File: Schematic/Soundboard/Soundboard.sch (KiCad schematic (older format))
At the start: 0 parts

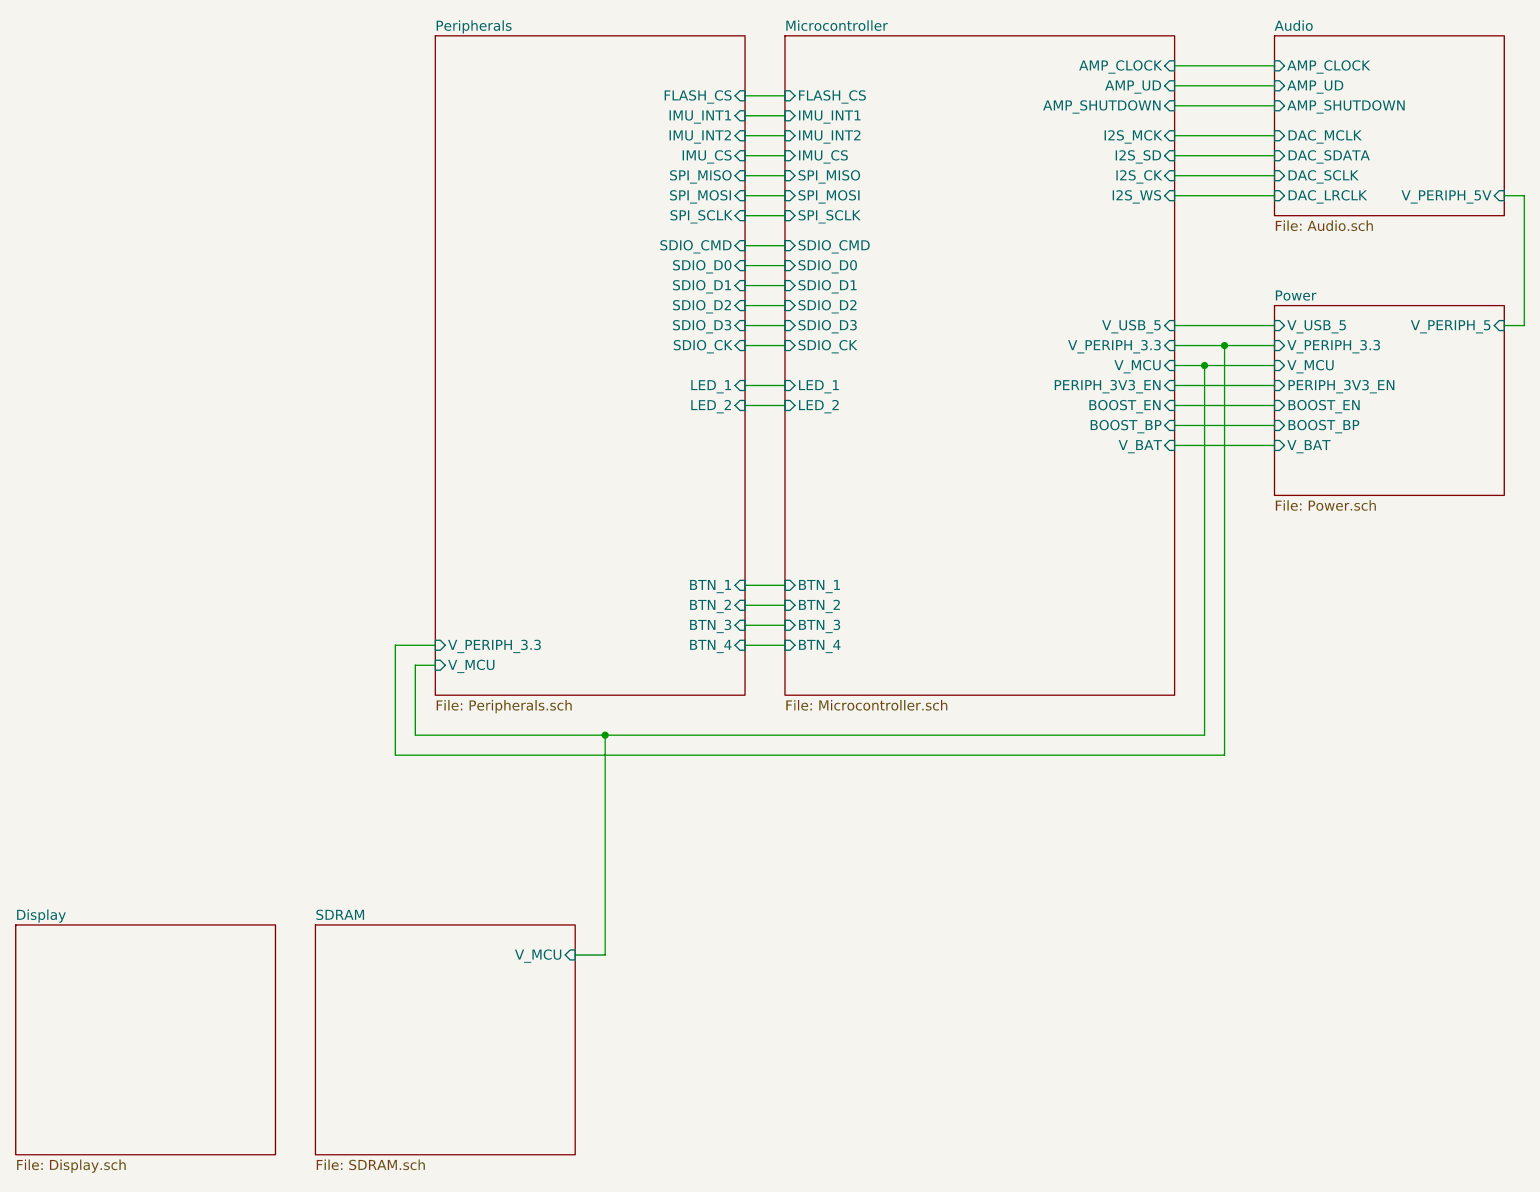
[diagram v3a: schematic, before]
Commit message: Choose display. Complete schematic
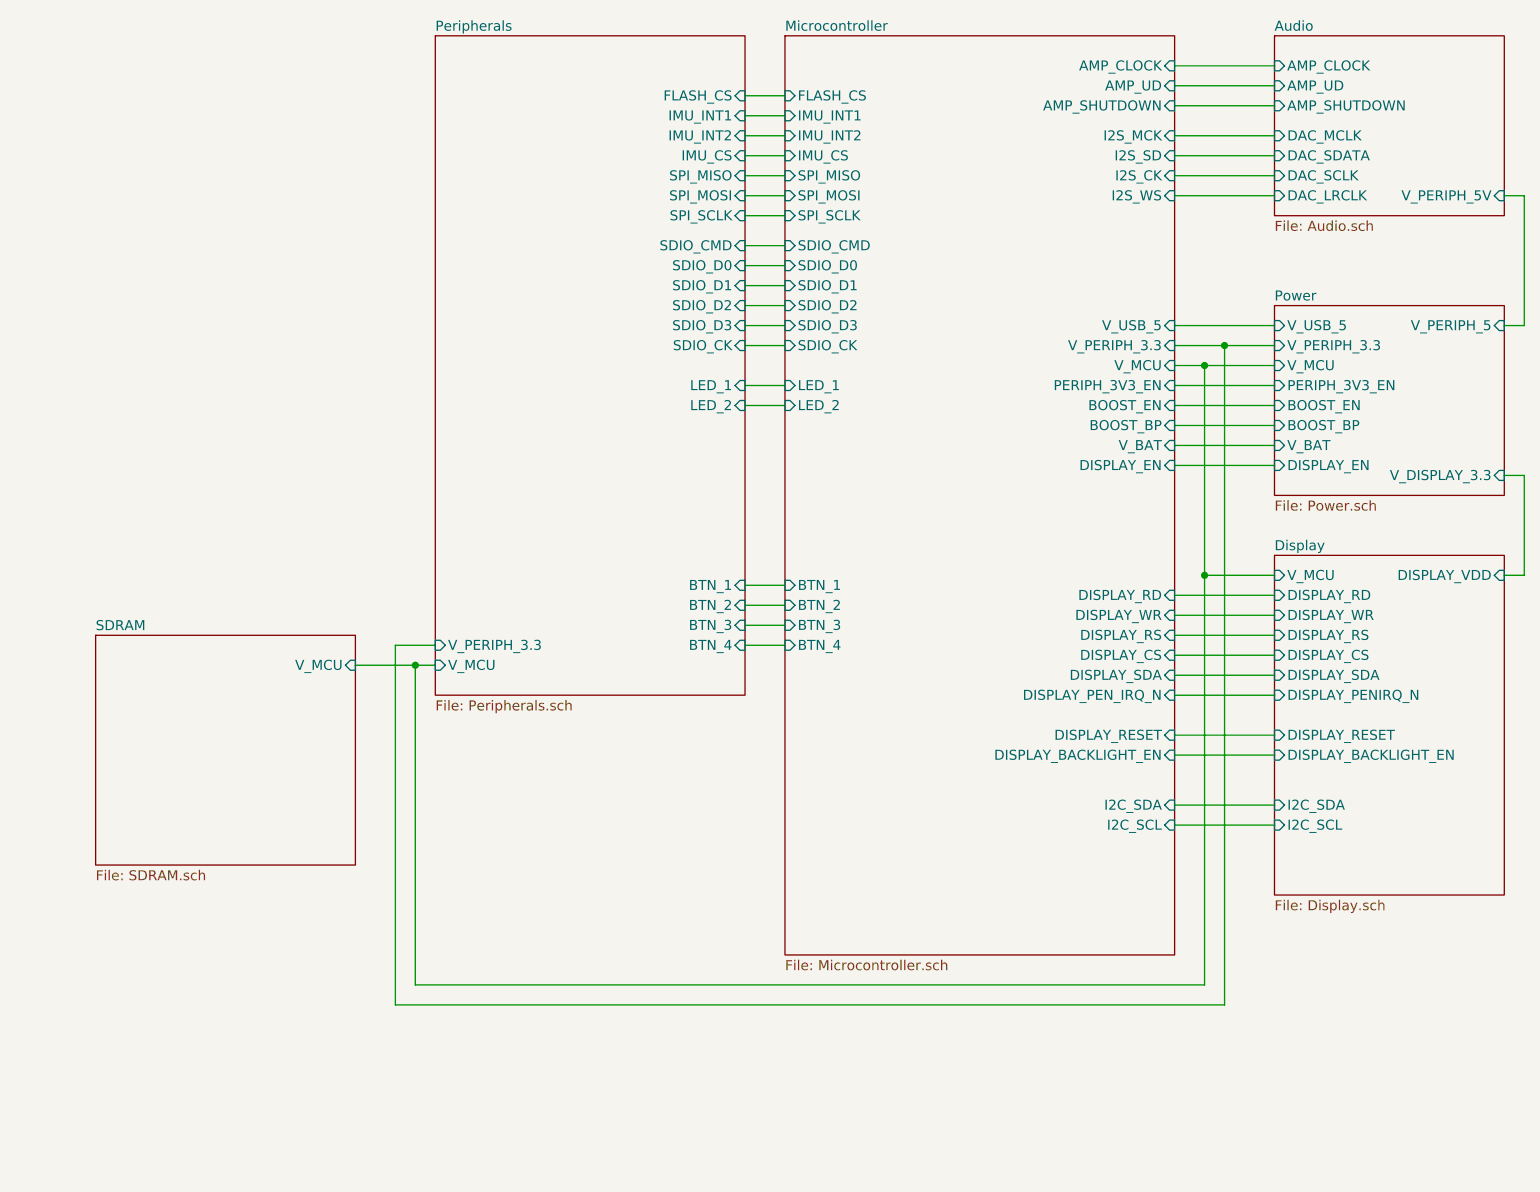
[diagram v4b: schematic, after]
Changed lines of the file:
@@
 F8 "V_MCU" I L 7300 3100 50
 F9 "V_BAT" I L 7300 3500 50
-$EndSheet
-$Sheet
-S 2500 5900 1300 1150
+F10 "V_DISPLAY_3.3" I R 8450 3650 50
+F11 "DISPLAY_EN" I L 7300 3600 50
+$EndSheet
+$Sheet
+S 1400 4450 1300 1150
 U 5F230DA4
 F0 "SDRAM" 50
 F1 "SDRAM.sch" 50
-F2 "V_MCU" I R 3800 6050 50
-$EndSheet
-$Sheet
-S 1000 5900 1300 1150
+F2 "V_MCU" I R 2700 4600 50
+$EndSheet
+$Sheet
+S 7300 4050 1150 1700
 U 5F230EC3
 F0 "Display" 50
 F1 "Display.sch" 50
+F2 "DISPLAY_RD" I L 7300 4250 50
+F3 "DISPLAY_WR" I L 7300 4350 50
+F4 "DISPLAY_RS" I L 7300 4450 50
+F5 "DISPLAY_CS" I L 7300 4550 50
+F6 "DISPLAY_SDA" I L 7300 4650 50
+F7 "DISPLAY_RESET" I L 7300 4950 50
+F8 "DISPLAY_VDD" I R 8450 4150 50
+F9 "I2C_SDA" I L 7300 5300 50
+F10 "I2C_SCL" I L 7300 5400 50
+F11 "DISPLAY_PENIRQ_N" I L 7300 4750 50
+F12 "DISPLAY_BACKLIGHT_EN" I L 7300 5050 50
+F13 "V_MCU" I L 7300 4150 50
 $EndSheet
 Wire Wire Line
@@
 Wire Wire Line
 	8450 2900 8550 2900
-$Sheet
-S 4850 1450 1950 3300
+Wire Wire Line
+	6800 1950 7300 1950
+Wire Wire Line
+	6800 2050 7300 2050
+Wire Wire Line
+	6800 2150 7300 2150
+Wire Wire Line
+	6800 2250 7300 2250
+Wire Wire Line
+	6800 1800 7300 1800
+Wire Wire Line
+	6800 1700 7300 1700
+Wire Wire Line
+	6800 1600 7300 1600
+Wire Wire Line
+	6800 2900 7300 2900
+Wire Wire Line
+	6800 3000 7050 3000
+Wire Wire Line
+	6800 3100 6950 3100
+Wire Wire Line
+	6800 3200 7300 3200
+Wire Wire Line
+	6800 3300 7300 3300
+Wire Wire Line
+	6800 3400 7300 3400
+$Sheet
+S 3100 1450 1550 3300
+U 5F4E88D1
+F0 "Peripherals" 50
+F1 "Peripherals.sch" 50
+F2 "V_PERIPH_3.3" I L 3100 4500 50
+F3 "V_MCU" I L 3100 4600 50
+F4 "IMU_INT1" I R 4650 1850 50
+F5 "IMU_INT2" I R 4650 1950 50
+F6 "IMU_CS" I R 4650 2050 50
+F7 "SPI_MISO" I R 4650 2150 50
+F8 "SPI_MOSI" I R 4650 2250 50
+F9 "SPI_SCLK" I R 4650 2350 50
+F10 "FLASH_CS" I R 4650 1750 50
+F11 "LED_1" I R 4650 3200 50
+F12 "LED_2" I R 4650 3300 50
+F13 "BTN_1" I R 4650 4200 50
+F14 "BTN_2" I R 4650 4300 50
+F15 "BTN_3" I R 4650 4400 50
+F16 "BTN_4" I R 4650 4500 50
+F17 "SDIO_D3" I R 4650 2900 50
+F18 "SDIO_D0" I R 4650 2600 50
+F19 "SDIO_D1" I R 4650 2700 50
+F20 "SDIO_D2" I R 4650 2800 50
+F21 "SDIO_CK" I R 4650 3000 50
+F22 "SDIO_CMD" I R 4650 2500 50
+$EndSheet
+Wire Wire Line
+	4650 4200 4850 4200
+Wire Wire Line
+	4650 4300 4850 4300
+Wire Wire Line
+	4650 4400 4850 4400
+Wire Wire Line
+	4650 4500 4850 4500
+Wire Wire Line
+	4650 3300 4850 3300
+Wire Wire Line
+	4650 3200 4850 3200
+Wire Wire Line
+	4650 3000 4850 3000
+Wire Wire Line
+	4650 2900 4850 2900
+Wire Wire Line
+	4650 2800 4850 2800
+Wire Wire Line
+	4650 2700 4850 2700
+Wire Wire Line
+	4650 2600 4850 2600
+Wire Wire Line
+	4650 2500 4850 2500
+Wire Wire Line
+	4650 2350 4850 2350
+Wire Wire Line
+	4650 2250 4850 2250
+Wire Wire Line
+	4650 2150 4850 2150
+Wire Wire Line
+	4650 2050 4850 2050
+Wire Wire Line
+	4650 1950 4850 1950
+Wire Wire Line
+	4650 1850 4850 1850
+Wire Wire Line
+	4650 1750 4850 1750
+Wire Wire Line
+	6950 3100 6950 4150
+Connection ~ 6950 3100
+Wire Wire Line
+	6950 3100 7300 3100
+Wire Wire Line
+	7050 3000 7050 6300
+Wire Wire Line
+	7050 6300 2900 6300
+Connection ~ 7050 3000
+Wire Wire Line
+	7050 3000 7300 3000
+Wire Wire Line
+	3000 4600 3100 4600
+Wire Wire Line
+	2900 6300 2900 4500
+Wire Wire Line
+	2900 4500 3100 4500
+Wire Wire Line
+	6800 3500 7300 3500
+Wire Wire Line
+	3000 4600 3000 6200
+Wire Wire Line
+	3000 6200 6950 6200
+$Sheet
+S 4850 1450 1950 4600
 U 5F0E03BF
 F0 "Microcontroller" 50
@@
 F33 "BTN_4" I L 4850 4500 50
 F34 "V_BAT" I R 6800 3500 50
-$EndSheet
-Wire Wire Line
-	6800 1950 7300 1950
-Wire Wire Line
-	6800 2050 7300 2050
-Wire Wire Line
-	6800 2150 7300 2150
-Wire Wire Line
-	6800 2250 7300 2250
-Wire Wire Line
-	6800 1800 7300 1800
-Wire Wire Line
-	6800 1700 7300 1700
-Wire Wire Line
-	6800 1600 7300 1600
-Wire Wire Line
-	6800 2900 7300 2900
-Wire Wire Line
-	6800 3000 7050 3000
-Wire Wire Line
-	6800 3100 6950 3100
-Wire Wire Line
-	6800 3200 7300 3200
-Wire Wire Line
-	6800 3300 7300 3300
-Wire Wire Line
-	6800 3400 7300 3400
-$Sheet
-S 3100 1450 1550 3300
-U 5F4E88D1
-F0 "Peripherals" 50
-F1 "Peripherals.sch" 50
-F2 "V_PERIPH_3.3" I L 3100 4500 50
-F3 "V_MCU" I L 3100 4600 50
-F4 "IMU_INT1" I R 4650 1850 50
-F5 "IMU_INT2" I R 4650 1950 50
-F6 "IMU_CS" I R 4650 2050 50
-F7 "SPI_MISO" I R 4650 2150 50
-F8 "SPI_MOSI" I R 4650 2250 50
-F9 "SPI_SCLK" I R 4650 2350 50
-F10 "FLASH_CS" I R 4650 1750 50
-F11 "LED_1" I R 4650 3200 50
-F12 "LED_2" I R 4650 3300 50
-F13 "BTN_1" I R 4650 4200 50
-F14 "BTN_2" I R 4650 4300 50
-F15 "BTN_3" I R 4650 4400 50
-F16 "BTN_4" I R 4650 4500 50
-F17 "SDIO_D3" I R 4650 2900 50
-F18 "SDIO_D0" I R 4650 2600 50
-F19 "SDIO_D1" I R 4650 2700 50
-F20 "SDIO_D2" I R 4650 2800 50
-F21 "SDIO_CK" I R 4650 3000 50
-F22 "SDIO_CMD" I R 4650 2500 50
-$EndSheet
-Wire Wire Line
-	4650 4200 4850 4200
-Wire Wire Line
-	4650 4300 4850 4300
-Wire Wire Line
-	4650 4400 4850 4400
-Wire Wire Line
-	4650 4500 4850 4500
-Wire Wire Line
-	4650 3300 4850 3300
-Wire Wire Line
-	4650 3200 4850 3200
-Wire Wire Line
-	4650 3000 4850 3000
-Wire Wire Line
-	4650 2900 4850 2900
-Wire Wire Line
-	4650 2800 4850 2800
-Wire Wire Line
-	4650 2700 4850 2700
-Wire Wire Line
-	4650 2600 4850 2600
-Wire Wire Line
-	4650 2500 4850 2500
-Wire Wire Line
-	4650 2350 4850 2350
-Wire Wire Line
-	4650 2250 4850 2250
-Wire Wire Line
-	4650 2150 4850 2150
-Wire Wire Line
-	4650 2050 4850 2050
-Wire Wire Line
-	4650 1950 4850 1950
-Wire Wire Line
-	4650 1850 4850 1850
-Wire Wire Line
-	4650 1750 4850 1750
-Wire Wire Line
-	6950 3100 6950 4950
-Wire Wire Line
-	6950 4950 3950 4950
-Connection ~ 6950 3100
-Wire Wire Line
-	6950 3100 7300 3100
-Wire Wire Line
-	7050 3000 7050 5050
-Wire Wire Line
-	7050 5050 2900 5050
-Connection ~ 7050 3000
-Wire Wire Line
-	7050 3000 7300 3000
-Wire Wire Line
-	3000 4950 3000 4600
-Wire Wire Line
-	3000 4600 3100 4600
-Wire Wire Line
-	2900 5050 2900 4500
-Wire Wire Line
-	2900 4500 3100 4500
-Wire Wire Line
-	3950 4950 3950 6050
-Wire Wire Line
-	3950 6050 3800 6050
-Connection ~ 3950 4950
-Wire Wire Line
-	3950 4950 3000 4950
-Wire Wire Line
-	6800 3500 7300 3500
+F35 "DISPLAY_RD" I R 6800 4250 50
+F36 "DISPLAY_CS" I R 6800 4550 50
+F37 "DISPLAY_SDA" I R 6800 4650 50
+F38 "DISPLAY_RS" I R 6800 4450 50
+F39 "DISPLAY_WR" I R 6800 4350 50
+F40 "DISPLAY_PEN_IRQ_N" I R 6800 4750 50
+F41 "DISPLAY_BACKLIGHT_EN" I R 6800 5050 50
+F42 "I2C_SDA" I R 6800 5300 50
+F43 "I2C_SCL" I R 6800 5400 50
+F44 "DISPLAY_RESET" I R 6800 4950 50
+F45 "DISPLAY_EN" I R 6800 3600 50
+$EndSheet
+Wire Wire Line
+	8450 3650 8550 3650
+Wire Wire Line
+	8550 3650 8550 4150
+Wire Wire Line
+	8550 4150 8450 4150
+Wire Wire Line
+	6800 3600 7300 3600
+Wire Wire Line
+	3000 4600 2700 4600
+Connection ~ 3000 4600
+Wire Wire Line
+	6800 4250 7300 4250
+Wire Wire Line
+	6800 4350 7300 4350
+Wire Wire Line
+	6800 4450 7300 4450
+Wire Wire Line
+	6800 4550 7300 4550
+Wire Wire Line
+	6800 4650 7300 4650
+Wire Wire Line
+	6800 4750 7300 4750
+Wire Wire Line
+	6800 4950 7300 4950
+Wire Wire Line
+	6800 5050 7300 5050
+Wire Wire Line
+	6800 5300 7300 5300
+Wire Wire Line
+	6800 5400 7300 5400
+Wire Wire Line
+	7300 4150 6950 4150
+Connection ~ 6950 4150
+Wire Wire Line
+	6950 4150 6950 6200
 $EndSCHEMATC
